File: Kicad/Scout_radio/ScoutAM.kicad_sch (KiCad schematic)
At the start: 92 parts, among them J1 Conn_01x07, J2 Conn_01x02, J3 PJ-342, J4 Conn_Coaxial, J5 Conn_01x02, Q1 AO3401A, Q2 2N7002, SW1 TC-6610-5-260G, SW2 TC-6610-5-260G, SW3 TC-6610-5-260G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

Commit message: Updated README.md
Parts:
- SW1, SW2, SW3, SW4, SW5, SW6: value TC-6610-5-260G -> B3FS; footprint Button_Switch_SMD:SW_Push_1P1T_NO_6x6mm_H9.5mm -> Scout:SW_Push_1P1T_NO_6x6mm_H9.5mm

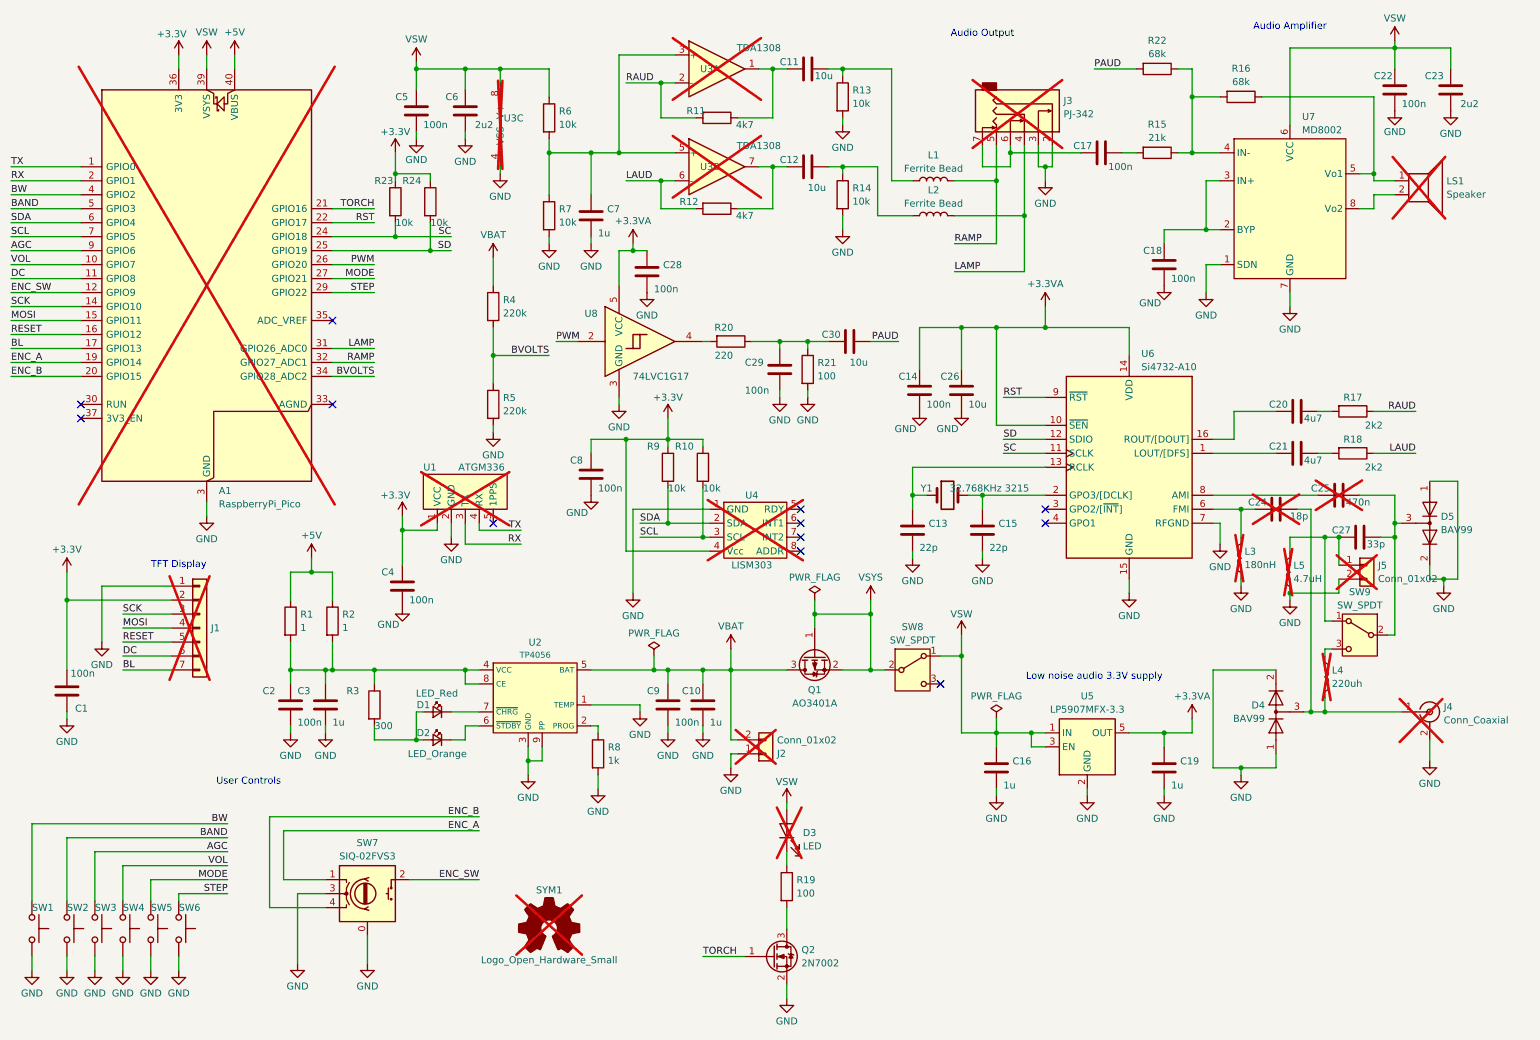
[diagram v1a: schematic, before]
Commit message: Added software folder
Added software folder with CircuitPython for testing
Fixed hardware cross of SDA and SCL to Si4732
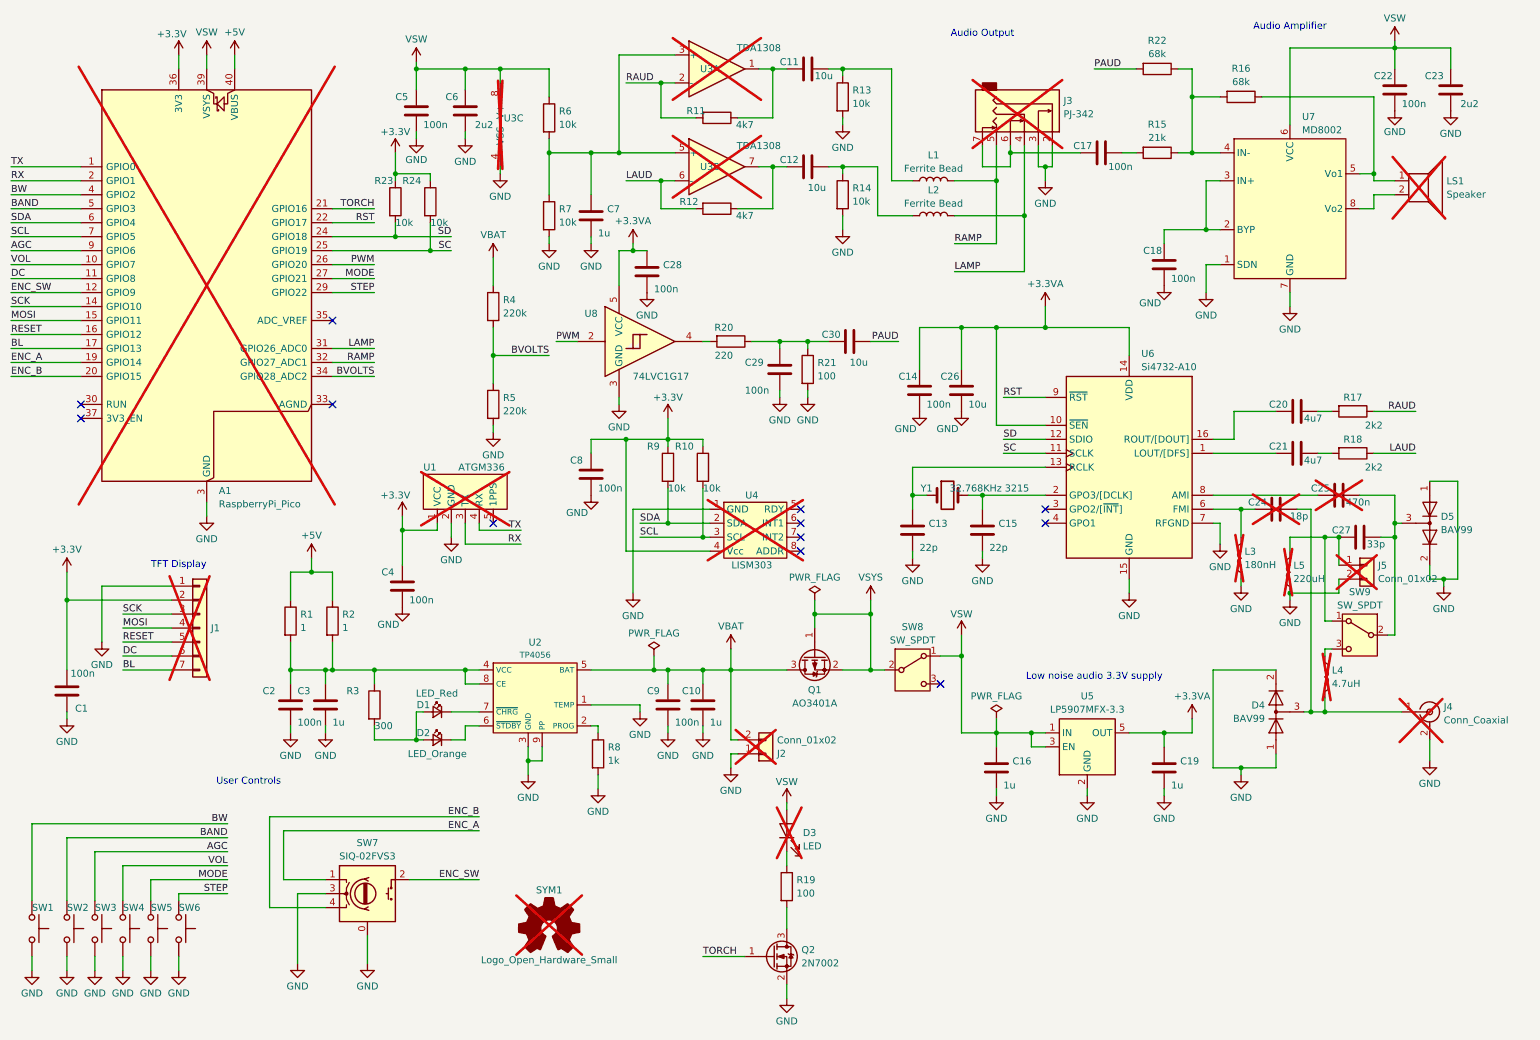
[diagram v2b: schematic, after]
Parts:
- L4: value 220uh -> 4.7uH
- L5: value 4.7uH -> 220uH
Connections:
- net SC: now also A1.25 (GPIO19), R24.2; no longer A1.24 (GPIO18), R23.2
- net SD: now also A1.24 (GPIO18), R23.2; no longer A1.25 (GPIO19), R24.2

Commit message: Recent changes
Sorry lost track of the changes. So created a new branch!
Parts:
- added R25, R26: 10k, Resistor_SMD:R_0603_1608Metric, symbol Device:R
- D1: value LED_Red -> LED_Blue
- R8: value 1k -> 2k
- U4: value LISM303 -> GY511; footprint Scout:LISM303 -> Scout:GY511; symbol Scout:LSM303 -> Scout:GY511
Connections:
- net +3.3V: now also U4.1 (Vin); no longer U4.4 (Vcc)
- net +5V: now also Q1.1 (G), R25.1
- net GND: now also U4.3 (GND), R25.2, R26.2; no longer U4.1 (GND)
- net SCL: now also U4.4 (SCL); no longer U4.3 (SCL)
- net SDA: now also U4.5 (SDA); no longer U4.2 (SDA)
- net TORCH: now also R26.1
- net VSYS: no longer names the net of Q1.2 (S), SW8.2 (B)
- net VSYS: no longer Q1.1 (G)
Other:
- moved on the sheet: D3, J2, Q2, R19
